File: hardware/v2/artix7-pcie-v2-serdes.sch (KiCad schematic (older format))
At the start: 23 parts, among them J4 USB3_A, J5 USB3_A_AS_PCIE, U1 XC7A75T-FGG484

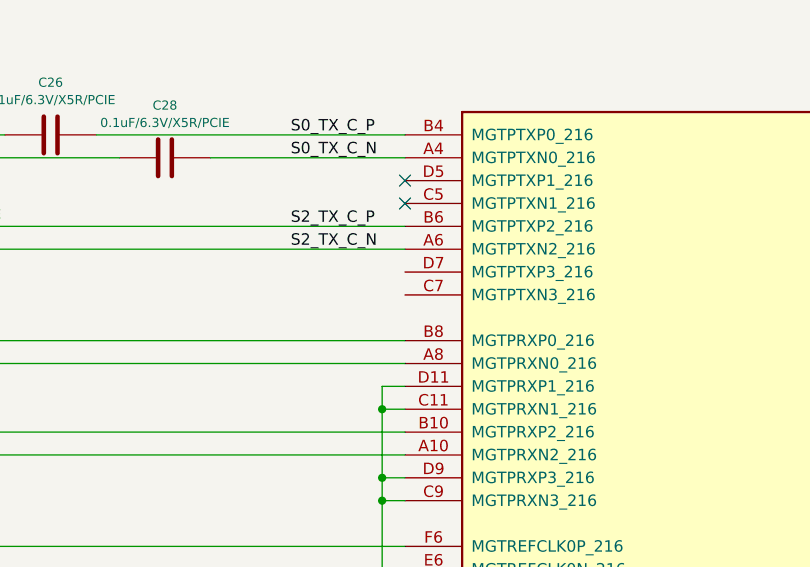
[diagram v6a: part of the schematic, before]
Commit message: v2 hardware: all tracks routed, erc/drc pass
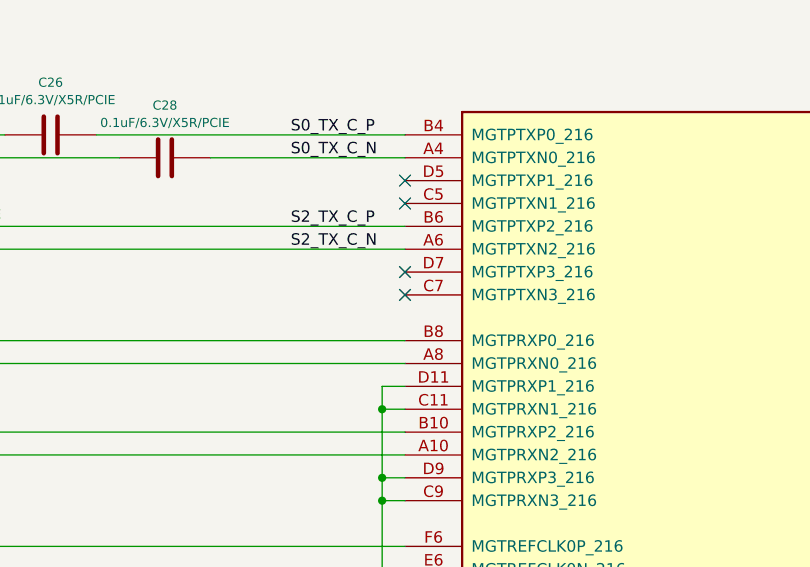
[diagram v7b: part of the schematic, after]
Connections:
- no-connect marks 2 -> 4
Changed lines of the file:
@@
 Wire Wire Line
 	7150 3400 7150 4000
+NoConn ~ 7250 2400
+NoConn ~ 7250 2500
 $EndSCHEMATC

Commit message: v2 hardware: j2_34 diff pairs matched, fix 0402 resistor packages, dropped paste from DNP resistors
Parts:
- R26, R27, R28, R43, R45: footprint tom-passives:C_0402_1005Metric -> tom-passives:R_0402_1005Metric
- R42, R44: footprint tom-passives:C_0402_1005Metric -> tom-passives:R_0402_1005Metric_NoPaste
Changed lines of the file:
@@
 F 0 "R26" V 1865 3050 40  0000 C CNN
 F 1 "0R" V 1941 3050 40  0000 C CNN
-F 2 "tom-passives:C_0402_1005Metric" V 1980 3050 30  0001 C CNN
+F 2 "tom-passives:R_0402_1005Metric" V 1980 3050 30  0001 C CNN
 F 3 "" H 2050 3050 30  0001 C CNN
 	1    2050 3050
@@
 F 0 "R27" V 1865 5350 40  0000 C CNN
 F 1 "0R" V 1941 5350 40  0000 C CNN
-F 2 "tom-passives:C_0402_1005Metric" V 1980 5350 30  0001 C CNN
+F 2 "tom-passives:R_0402_1005Metric" V 1980 5350 30  0001 C CNN
 F 3 "" H 2050 5350 30  0001 C CNN
 	1    2050 5350
@@
 F 0 "R28" V 8165 6000 40  0000 C CNN
 F 1 "100R/1%" V 8241 6000 40  0000 C CNN
-F 2 "tom-passives:C_0402_1005Metric" V 8280 6000 30  0001 C CNN
+F 2 "tom-passives:R_0402_1005Metric" V 8280 6000 30  0001 C CNN
 F 3 "" H 8350 6000 30  0001 C CNN
 	1    8350 6000
@@
 F 0 "R44" V 2565 5950 40  0000 C CNN
 F 1 "DNP" V 2641 5950 40  0000 C CNN
-F 2 "tom-passives:C_0402_1005Metric" V 2680 5950 30  0001 C CNN
+F 2 "tom-passives:R_0402_1005Metric_NoPaste" V 2680 5950 30  0001 C CNN
 F 3 "" H 2750 5950 30  0001 C CNN
 	1    2750 5950
@@
 F 0 "R43" V 1965 5950 40  0000 C CNN
 F 1 "0R" V 2041 5950 40  0000 C CNN
-F 2 "tom-passives:C_0402_1005Metric" V 2080 5950 30  0001 C CNN
+F 2 "tom-passives:R_0402_1005Metric" V 2080 5950 30  0001 C CNN
 F 3 "" H 2150 5950 30  0001 C CNN
 	1    2150 5950
@@
 F 0 "R42" V 1965 5650 40  0000 C CNN
 F 1 "DNP" V 2041 5650 40  0000 C CNN
-F 2 "tom-passives:C_0402_1005Metric" V 2080 5650 30  0001 C CNN
+F 2 "tom-passives:R_0402_1005Metric_NoPaste" V 2080 5650 30  0001 C CNN
 F 3 "" H 2150 5650 30  0001 C CNN
 	1    2150 5650
@@
 F 0 "R45" V 2665 5650 40  0000 C CNN
 F 1 "0R" V 2741 5650 40  0000 C CNN
-F 2 "tom-passives:C_0402_1005Metric" V 2780 5650 30  0001 C CNN
+F 2 "tom-passives:R_0402_1005Metric" V 2780 5650 30  0001 C CNN
 F 3 "" H 2850 5650 30  0001 C CNN
 	1    2850 5650
